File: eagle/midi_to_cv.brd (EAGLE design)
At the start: 100 x 80 mm, 46 parts, among them IC2 4504N, IC3 4099N, U1 ATMEGA328P_PDIP

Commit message: a manual start
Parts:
- moved R12 22.9 mm to (77.5, 49.5), turned to 0 degrees
- moved R19 10.0 mm to (75.6, 5.08), turned to 0 degrees
- moved R20 9.25 mm to (52.7, 6.35)
- moved MIDI_IN 8.98 mm to (7.62, 72.4), turned to 0 degrees
- moved R21 8.03 mm to (49.5, 8.89)
- moved IC3 7.73 mm to (63.5, 43.2)
- moved R1 7.73 mm to (17.8, 73.7)
- moved JP2 7.73 mm to (55.9, 19.1)
- moved R11 7.62 mm to (76.2, 30.5)
- moved OK2 7.41 mm to (8.89, 57.1)
- moved R17 6.84 mm to (48.3, 12.7)
- moved R16 6.84 mm to (44.5, 15.2)
- moved JP3 6.48 mm to (79.4, 19.1)
- moved R10 6.48 mm to (72.4, 29.2)
- moved D2 6.35 mm to (7.62, 64.8)
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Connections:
- net N$13: now also U1.25; no longer U1.23
- net N$25: now also U1.23; no longer U1.25
- net N$37: now also IC3.4; no longer IC3.3
- net N$38: now also IC3.3; no longer IC3.4
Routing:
- net N$61: track 0.00 -> 46.1 mm, vias 0 -> 2
- net +12V: track 0.00 -> 43.7 mm, vias 0 -> 2
- net N$30: track 0.00 -> 43.6 mm
- net N$32: track 0.00 -> 39.2 mm
- net +5V: track 0.00 -> 38.9 mm, vias 0 -> 2
- net N$38: track 0.00 -> 38.6 mm, vias 0 -> 2
- net N$13: track 0.00 -> 33.2 mm
- net N$31: track 0.00 -> 29.7 mm
- net N$23: track 0.00 -> 26.8 mm
- net N$37: track 0.00 -> 22.9 mm
- net N$25: track 0.00 -> 22.4 mm
- net GND: track 0.00 -> 20.1 mm, vias 0 -> 2
- net N$36: track 0.00 -> 19.3 mm
- net N$35: track 0.00 -> 15.6 mm
- net N$33: track 0.00 -> 14.5 mm

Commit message: routed
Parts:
- moved R21 17.9 mm to (67.3, 10.8)
- moved R20 14.7 mm to (67.3, 8.26)
- moved R19 8.28 mm to (67.3, 5.71)
- moved R18 7.24 mm to (67.3, 3.17)
- moved PWR1 3.81 mm to (91.4, 67.3)
- moved PAD11 2.54 mm to (43.2, 41.9)
- moved R17 2.54 mm to (45.7, 12.7)
- moved MIDI_IN 1.91 mm to (7.62, 74.3)
- moved R5 1.91 mm to (7.62, 69.2)
- moved R11 1.42 mm to (74.9, 29.8)
- moved D2 1.27 mm to (7.62, 66.0)
- moved OK2 1.27 mm to (8.89, 58.4)
- moved R10 1.27 mm to (71.1, 29.2)
- moved R16 1.27 mm to (45.7, 15.2)
- moved R3 0.64 mm to (55.2, 30.5)
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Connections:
- removed net N$42: JP3.3, R20.2
- new net N$34: JP3.5, R20.2
- net N$37: now also IC3.3; no longer IC3.4
- net N$38: now also IC3.4; no longer IC3.3
- net N$40: now also JP3.1; no longer JP3.7
- net N$41: now also JP3.3; no longer JP3.5
- net N$51: now also JP3.7; no longer JP3.1
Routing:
- net +5V: track 38.9 -> 420.7 mm, vias 2 -> 4
- net GND: track 20.1 -> 195.6 mm
- net +12V: track 43.7 -> 140.3 mm
- net N$56: track 0.00 -> 48.5 mm
- net N$57: track 0.00 -> 40.3 mm
- net N$26: track 0.00 -> 37.5 mm
- net N$15: track 0.00 -> 34.1 mm, vias 0 -> 2
- net N$24: track 0.00 -> 32.4 mm
- net N$59: track 0.00 -> 32.4 mm
- net N$58: track 0.00 -> 32.2 mm
- net N$21: track 0.00 -> 31.2 mm
- net N$2: track 0.00 -> 28.5 mm
- net N$14: track 0.00 -> 28.4 mm
- net N$40: track 0.00 -> 24.3 mm
- net N$17: track 0.00 -> 23.2 mm
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
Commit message: cutout
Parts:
- removed PAD11, PAD14: gate LED, wirepad:2,54/0,9
- added LED: 22-23-2021, con-molex:22-23-2021
- moved C7 12.7 mm to (80.0, 55.2), turned to 0 degrees
- moved R17 8.64 mm to (37.5, 15.2), turned to 270 degrees
- moved MIDI_IN 8.28 mm to (15.9, 73.7), turned to 270 degrees
- moved R1 7.62 mm to (25.4, 73.7)
- moved C3 7.41 mm to (43.2, 52.1), turned to 0 degrees
- moved R11 6.38 mm to (81.3, 29.2)
- moved C5 5.85 mm to (80.0, 59.1), turned to 0 degrees
- moved R16 5.85 mm to (40.0, 16.5), turned to 270 degrees
- moved R10 5.71 mm to (76.8, 29.2)
- moved PAD12 5.24 mm to (30.5, 71.1)
- moved R4 5.08 mm to (40.6, 39.4), turned to 90 degrees
- moved R12 5.08 mm to (82.5, 49.5)
- moved R14 4.49 mm to (33.7, 31.1)
- moved R8 4.44 mm to (67.9, 29.2)
- moved C4 4.02 mm to (80.0, 74.9), turned to 0 degrees
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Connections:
- removed net N$26: C4.-, C5.-, C6.2, C7.2, PWR1.3, PWR1.4, PWR1.5, PWR1.6, PWR1.7, PWR1.8
- net GND: now also C4.-, C5.-, C6.2, C7.2, LED.1, PWR1.3, PWR1.4, PWR1.5, PWR1.6, PWR1.7, PWR1.8; no longer PAD14.1
- net N$11: now also LED.2; no longer PAD11.1
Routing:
- net +5V: track 420.7 -> 258.0 mm
- net N$26: track 37.5 -> 0.00 mm
- net GND: track 195.6 -> 226.4 mm
- net N$29: track 17.4 -> 34.5 mm
- net N$2: track 28.5 -> 12.0 mm
- net +12V: track 140.3 -> 125.4 mm
- net N$28: track 11.5 -> 25.8 mm
- net N$55: track 13.4 -> 3.33 mm
- net N$54: track 13.3 -> 6.42 mm
- net N$15: track 34.1 -> 39.9 mm, vias 2 -> 0
- net N$11: track 5.08 -> 10.6 mm
- net N$14: track 28.4 -> 32.3 mm
- net N$19: track 7.50 -> 11.4 mm
- net N$22: track 22.0 -> 25.5 mm
- net N$16: track 9.66 -> 6.32 mm
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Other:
- board size 100 x 80 mm -> 100.3 x 80 mm

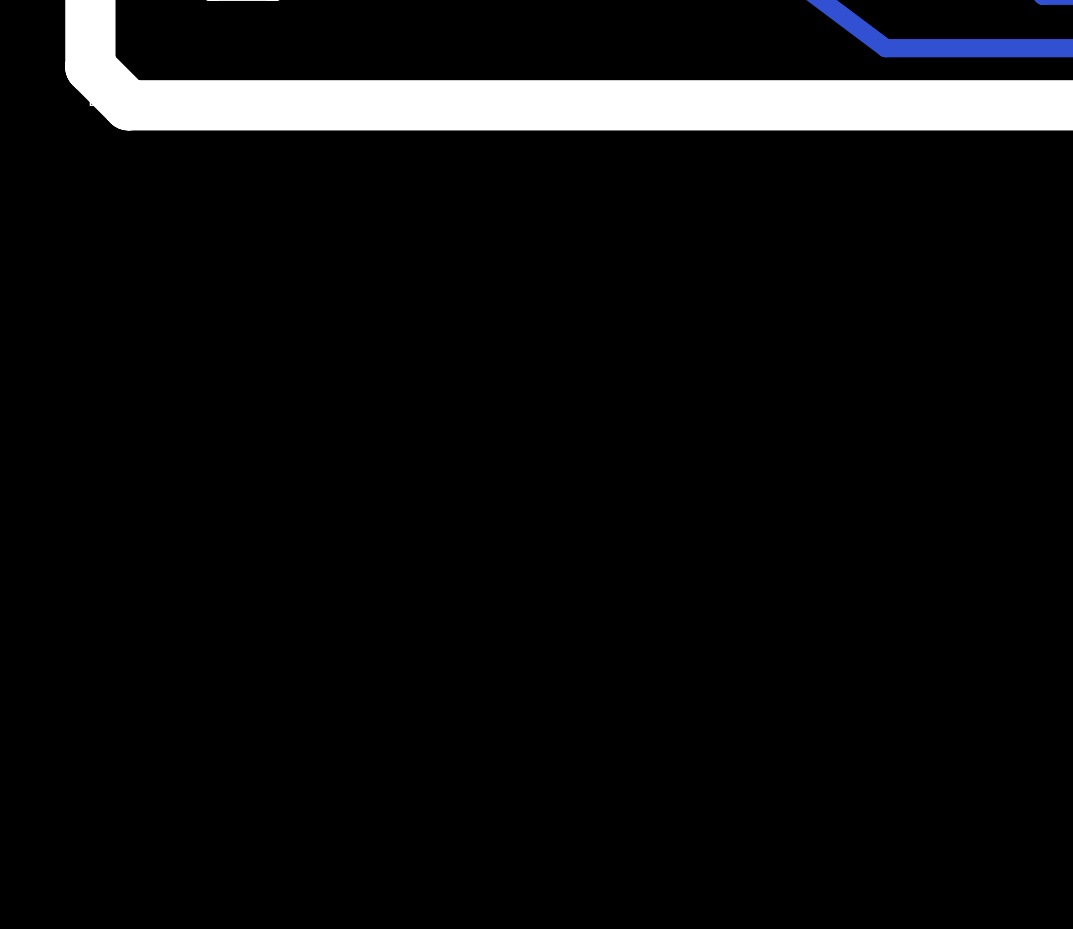
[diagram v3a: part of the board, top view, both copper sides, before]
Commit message: created the device for ad8804 12ch dac
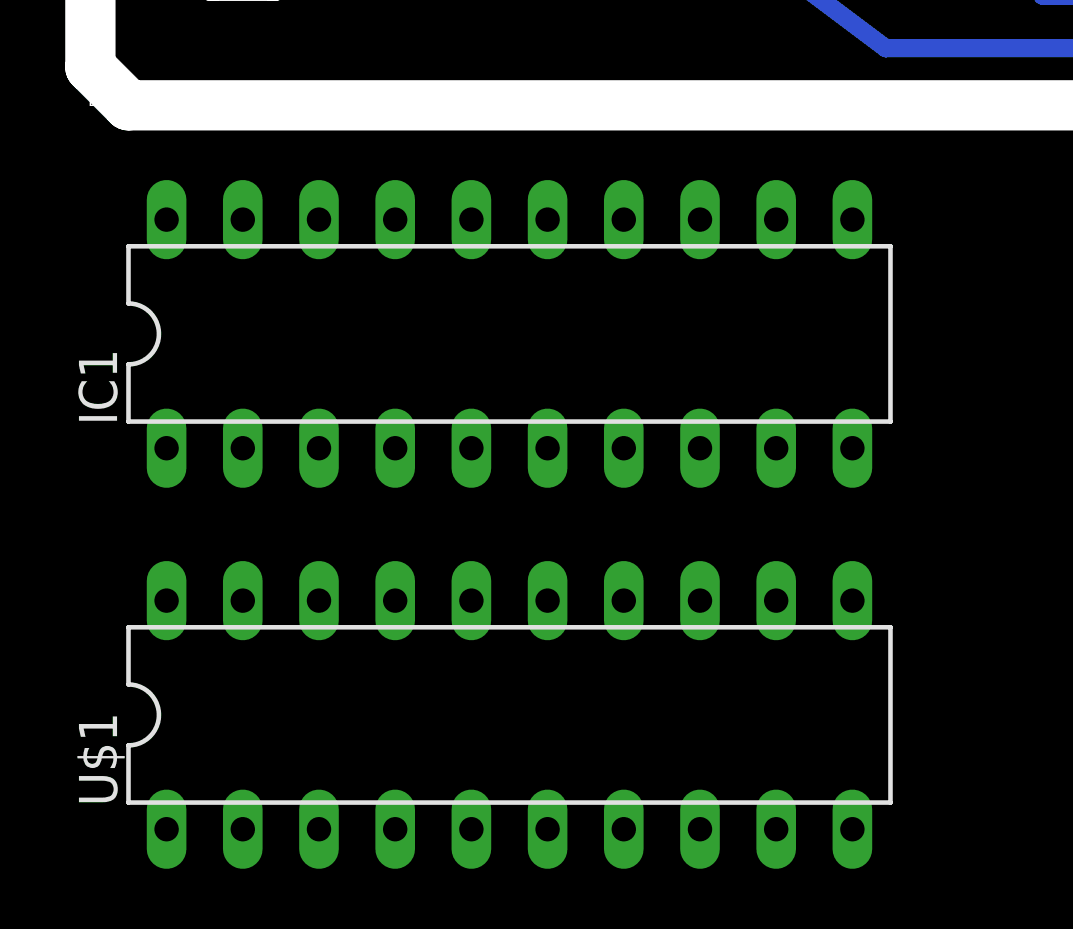
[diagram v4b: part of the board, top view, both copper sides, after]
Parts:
- added IC1: (no value), ic-package:DIL20
- added U$1: AD8804, ic-package:DIL20
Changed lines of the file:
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@@
 <?xml version="1.0" encoding="utf-8"?>
 <!DOCTYPE eagle SYSTEM "eagle.dtd">
-<eagle version="7.2.0">
+<eagle version="7.1.0">
 <drawing>
 <settings>
@@
 <attribute name="OC_FARNELL" value="1462926" x="45.72" y="44.45" size="1.778" layer="27" rot="R270" display="off"/>
 </element>
+<element name="IC1" library="ic-package" package="DIL20" value="" x="13.97" y="-7.62"/>
+<element name="U$1" library="ic-package" package="DIL20" value="AD8804" x="13.97" y="-20.32"/>
 </elements>
 <signals>

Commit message: midi thru
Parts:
- removed IC2: 4504N, 45xx:DIL16
- removed IC3: 4099N, 40xx:DIL16
- removed JP2, JP3: (no value), pinhead:1X08
- removed R10, R11, R12, R13, R14, R16, R17, R18, R19, R20, R21, R3, R7, R8, R9: 1k, rcl:0207/10
- removed U$11: TLV5628C/I, Texas Instruments_By_element14_Batch_1:DIP16
- added IC4, IC5: TL074P, linear:DIL14
- added MIDI_OUT_THRU1: 22-23-2031, con-molex:22-23-2031
- IC1: value (none) -> TL074P; device ic-package:DIL20 -> linear:DIL14
- R2: value 1k -> 220
- moved R2 121.7 mm to (6.35, -82.5), turned to 0 degrees
- moved IC1 13.3 mm to (10.2, -20.3)
- moved U$1 12.7 mm to (14.0, -7.62)
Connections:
- removed net N$13: IC2.7, U1.25
- removed net N$14: U$11.5, U1.13
- removed net N$15: U$11.12, U1.16
- removed net N$16: JP3.4, R11.2
- removed net N$21: JP3.2, R12.2
- removed net N$22: JP2.7, R13.2
- removed net N$23: IC2.5, U1.24
- removed net N$24: JP2.5, R14.2
- removed net N$25: IC2.3, U1.23
- removed net N$27: U$11.4, U1.14
- removed net N$28: JP2.3, R16.2
- removed net N$29: JP2.1, R17.2
- removed net N$30: IC2.9, U1.28
- removed net N$31: IC2.14, U1.26
- removed net N$32: IC2.11, U1.27
- removed net N$33: IC2.6, IC3.5
- removed net N$34: JP3.5, R20.2
- removed net N$35: IC2.4, IC3.6
- removed net N$36: IC2.2, IC3.7
- removed net N$37: IC2.10, IC3.3
- removed net N$38: IC2.12, IC3.4
- removed net N$39: IC3.9, R2.1
- removed net N$40: JP3.1, R18.2
- removed net N$41: JP3.3, R19.2
- removed net N$44: IC3.10, R3.1
- removed net N$45: IC3.11, R7.1
- removed net N$46: IC3.12, R8.1
- removed net N$47: IC3.13, R9.1
- removed net N$48: IC3.14, R10.1
- removed net N$49: IC3.15, R11.1
- removed net N$50: IC3.1, R12.1
- removed net N$51: JP3.7, R21.2
- removed net N$52: R13.1, U$11.2
- removed net N$53: R14.1, U$11.1
- removed net N$54: R16.1, U$11.16
- removed net N$55: R17.1, U$11.15
- removed net N$56: R18.1, U$11.7
- removed net N$57: R19.1, U$11.8
- removed net N$58: R20.1, U$11.9
- removed net N$59: R21.1, U$11.10
- removed net N$61: IC2.15, IC3.2
- new net V+: IC1.4, IC4.4, IC5.4
- new net V-: IC1.11, IC4.11, IC5.11
- net +12V: no longer IC2.16, IC3.16
- net +5V: now also R2.1, U$1.1, U$1.20; no longer IC2.1, IC2.13, U$11.11, U$11.14, U$11.6
- net GND: now also MIDI_OUT_THRU1.3, U$1.10, U$1.11; no longer IC2.8, IC3.8, U$11.13, U$11.3
- net N$12: now also MIDI_OUT_THRU1.2, U1.3; no longer JP3.6, R10.2
- net N$3: now also U$1.8, U1.23; no longer JP2.8, R2.2
- net N$6: now also U$1.9, U1.24; no longer JP2.6, R3.2
- net N$7: now also U$1.12, U1.25; no longer JP2.4, R7.2
- net N$8: now also U$1.13, U1.26; no longer JP2.2, R8.2
- net N$9: now also MIDI_OUT_THRU1.1, R2.2; no longer JP3.8, R9.2
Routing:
- net N$56: track 48.5 -> 0.00 mm
- net N$61: track 44.7 -> 0.00 mm, vias 2 -> 0
- net N$57: track 40.3 -> 0.00 mm
- net N$15: track 39.9 -> 0.00 mm
- net N$30: track 38.4 -> 0.00 mm
- net N$29: track 34.5 -> 0.00 mm
- net N$32: track 34.3 -> 0.00 mm
- net +5V: track 258.0 -> 223.8 mm
- net GND: track 226.4 -> 193.1 mm, vias 2 -> 0
- net N$59: track 32.4 -> 0.00 mm
- net N$14: track 32.3 -> 0.00 mm
- net N$58: track 32.2 -> 0.00 mm
- net N$24: track 32.1 -> 0.00 mm
- net N$13: track 31.6 -> 0.00 mm
- net N$21: track 30.5 -> 0.00 mm
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
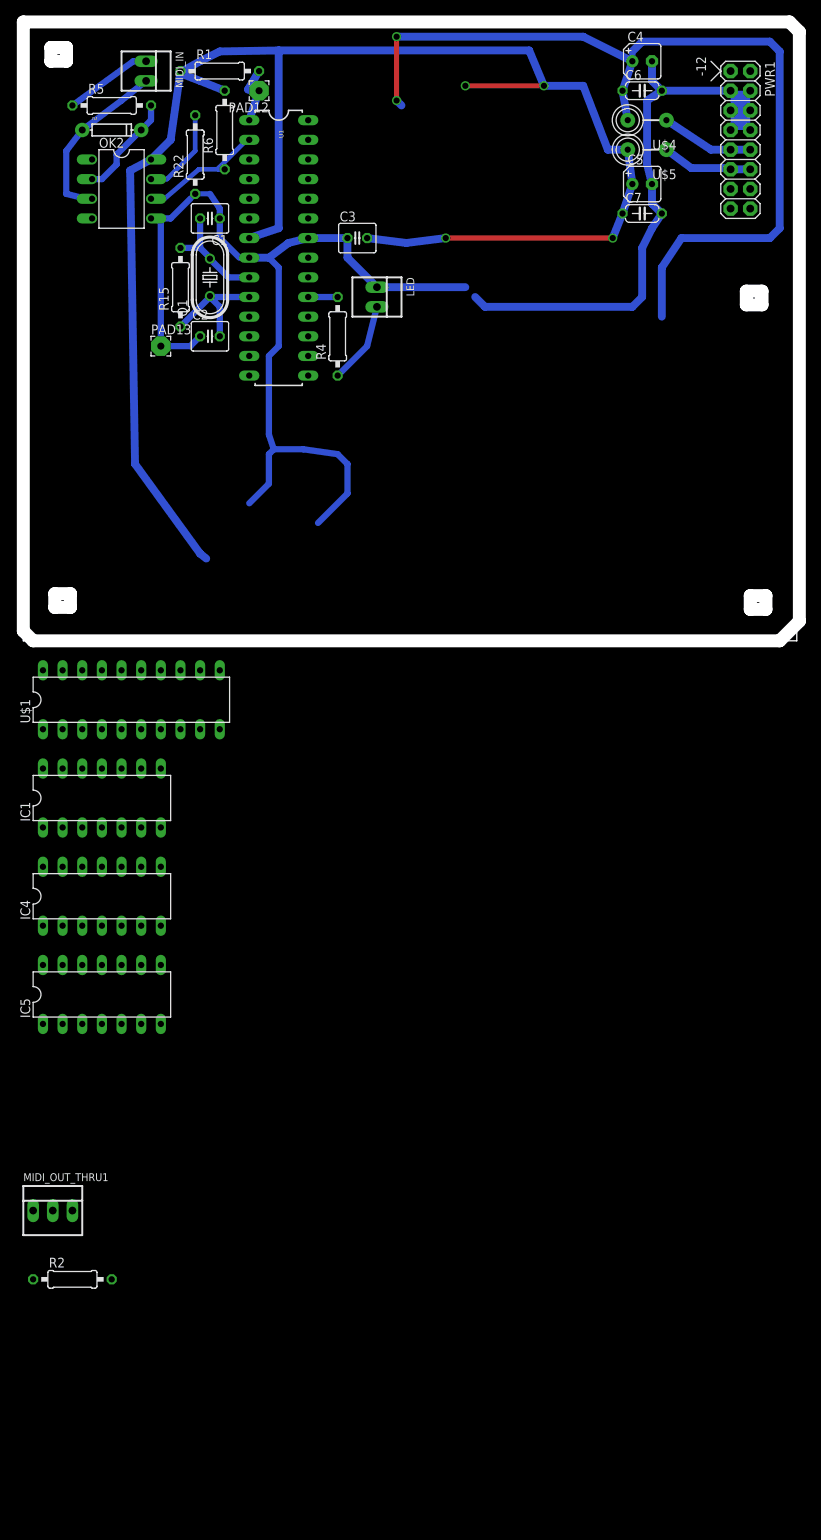
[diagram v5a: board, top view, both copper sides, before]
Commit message: first opamps
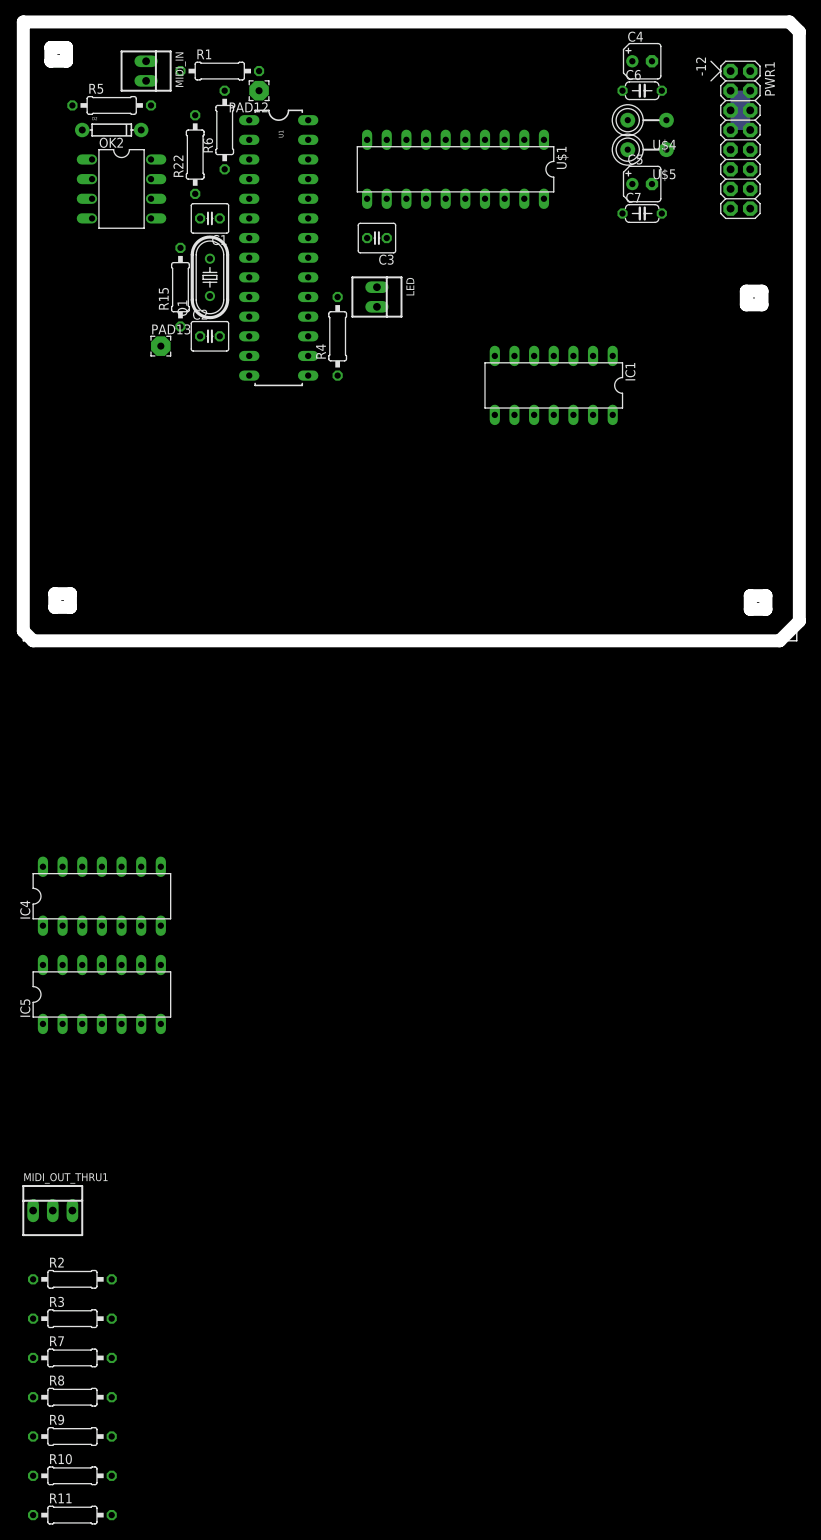
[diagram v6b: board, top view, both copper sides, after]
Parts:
- added R10, R9: 1k8, rcl:0207/10
- added R11, R3, R8: 1k, rcl:0207/10
- added R7: 6k8, rcl:0207/10
- moved U$1 80.4 mm to (55.9, 61.0), turned to 180 degrees
- moved IC1 79.1 mm to (68.6, 33.0), turned to 180 degrees
- moved C3 2.54 mm to (45.7, 52.1), turned to 180 degrees
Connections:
- new net N$13: IC1.2, IC1.9, R3.2, R7.1
- new net N$14: IC1.3, IC1.5, U$1.2
- new net N$15: IC1.6, R8.2, R9.1
- new net N$16: IC1.7, R9.2
- new net N$21: IC1.13, R10.1, R11.2
- new net N$22: IC1.10, U$1.3
- new net N$23: IC1.14, R10.2
- net +5V: now also R7.2
- net GND: now also R11.1, R3.1, R8.1
- net N$3: now also U1.26; no longer U1.23
- net N$6: now also U1.25; no longer U1.24
- net N$7: now also U1.23; no longer U1.25
- net N$8: now also U1.24; no longer U1.26
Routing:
- net +5V: track 223.8 -> 0.00 mm, vias 4 -> 0
- net GND: track 193.1 -> 0.00 mm
- net +12V: track 116.7 -> 0.00 mm, vias 2 -> 0
- net N$17: track 22.8 -> 0.00 mm
- net N$20: track 16.6 -> 0.00 mm
- net N$5: track 16.3 -> 0.00 mm
- net N$4: track 14.4 -> 0.00 mm
- net N$18: track 13.4 -> 0.00 mm
- net N$62: track 12.0 -> 0.00 mm
- net N$2: track 12.0 -> 0.00 mm
- net N$60: track 11.8 -> 0.00 mm
- net N$19: track 11.4 -> 0.00 mm
- net N$11: track 10.6 -> 0.00 mm
- net N$1: track 8.23 -> 0.00 mm
- net N$10: track 3.81 -> 0.00 mm
